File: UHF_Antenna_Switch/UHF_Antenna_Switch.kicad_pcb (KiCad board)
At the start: 2 copper layers, 157.2 x 60 mm, 49 parts, among them J1 Conn_N_Type_Female, J2 Conn_SO-239, J3 Conn_SMA_Female, J4 Screw_Terminal_01x04, J5 Conn_02x03_Odd_Even, K1 HF3-51, K2 HF3-51, Q2 2N7002, Q3 2N7002, SW1 SW_SP3T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

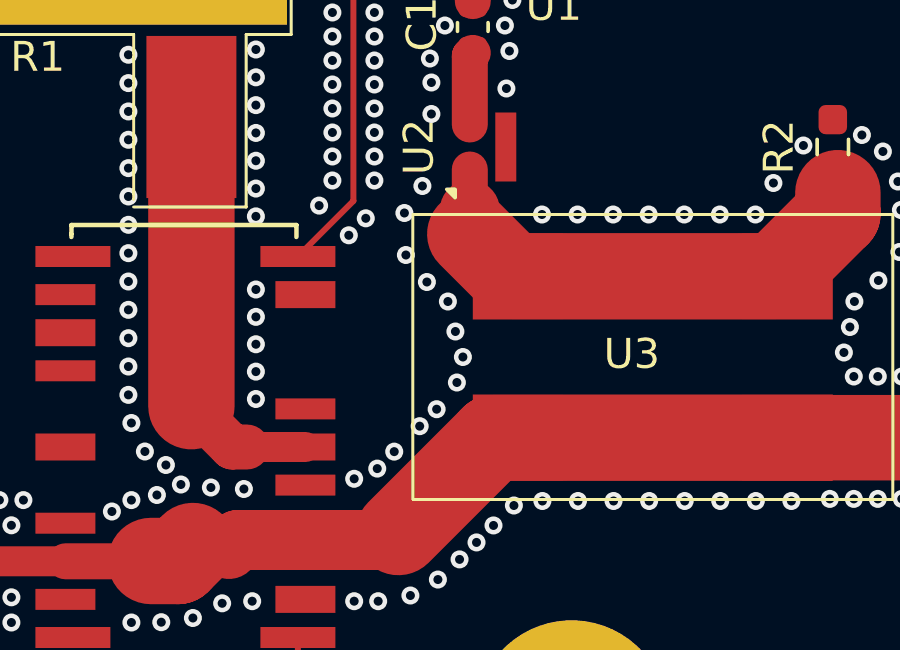
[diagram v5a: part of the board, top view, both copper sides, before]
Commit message: fix(pcb): DRC rule about intentional shorted nets in RF coupler
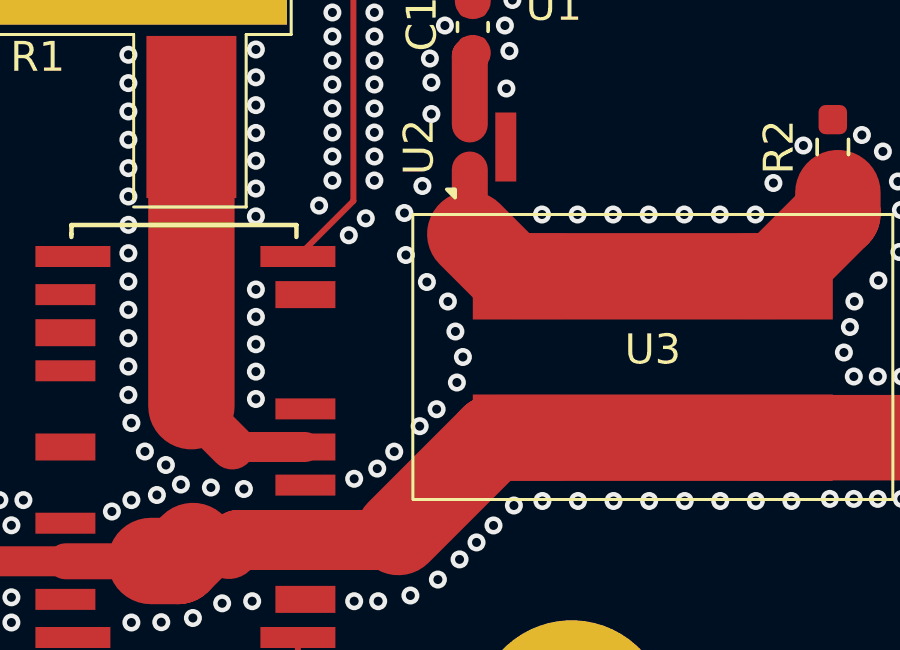
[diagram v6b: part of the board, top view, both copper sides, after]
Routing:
- net Net-(U3-COUPLED_OUT): track 8.22 -> 7.32 mm
